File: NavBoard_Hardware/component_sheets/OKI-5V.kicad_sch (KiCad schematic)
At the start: 4 parts, among them U1 OKI-5V

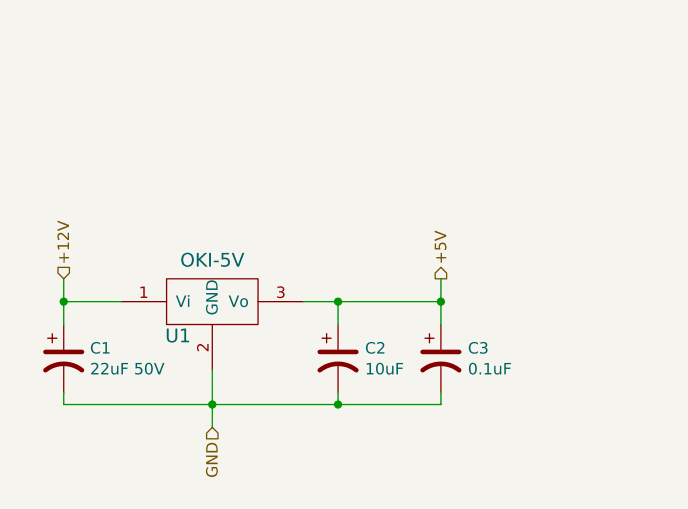
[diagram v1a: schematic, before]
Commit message: Added Information To Voltage Regulator Component Sheets, Improved Schematic Review 1 Powerpoint
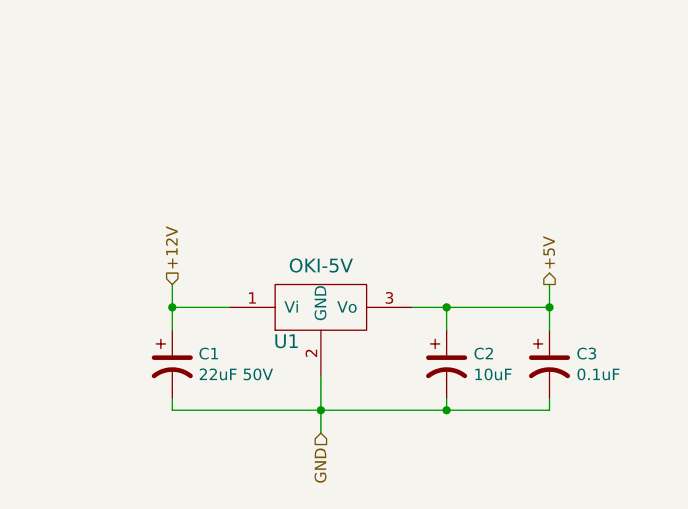
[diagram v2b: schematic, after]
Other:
- company: (none) -> Missouri S&T Mars Rover Design Team
- title: (none) -> OKI 5V Voltage Regulator
- moved on the sheet: C1, C2, C3, U1
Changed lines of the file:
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@@
 (kicad_sch (version 20211123) (generator eeschema)
   (paper "A4")
-  (junction (at 146.05 101.6) (diameter 0) (color 0 0 0 0)
+  (title_block
+    (title "OKI 5V Voltage Regulator")
+    (company "Missouri S&T Mars Rover Design Team")
+    (comment 1 "OKI 5V Voltage Regulator")
+    (comment 2 "Provides Stable 5V From 12V Input")
   )
-  (junction (at 146.05 90.17) (diameter 0) (color 0 0 0 0)
+  (junction (at 158.115 102.235) (diameter 0) (color 0 0 0 0)
   )
-  (junction (at 132.08 101.6) (diameter 0) (color 0 0 0 0)
+  (junction (at 158.115 90.805) (diameter 0) (color 0 0 0 0)
   )
-  (junction (at 115.57 90.17) (diameter 0) (color 0 0 0 0)
+  (junction (at 144.145 102.235) (diameter 0) (color 0 0 0 0)
   )
-  (junction (at 157.48 90.17) (diameter 0) (color 0 0 0 0)
+  (junction (at 127.635 90.805) (diameter 0) (color 0 0 0 0)
   )
-  (wire (pts (xy 115.57 87.63) (xy 115.57 90.17))
+  (junction (at 169.545 90.805) (diameter 0) (color 0 0 0 0)
+  )
+  (wire (pts (xy 127.635 88.265) (xy 127.635 90.805))
     (stroke (width 0) (type default) (color 0 0 0 0))
   )
-  (wire (pts (xy 157.48 101.6) (xy 157.48 100.33))
+  (wire (pts (xy 169.545 102.235) (xy 169.545 100.965))
     (stroke (width 0) (type default) (color 0 0 0 0))
   )
-  (wire (pts (xy 115.57 100.33) (xy 115.57 101.6))
+  (wire (pts (xy 127.635 100.965) (xy 127.635 102.235))
     (stroke (width 0) (type default) (color 0 0 0 0))
   )
-  (wire (pts (xy 146.05 101.6) (xy 157.48 101.6))
+  (wire (pts (xy 158.115 102.235) (xy 169.545 102.235))
     (stroke (width 0) (type default) (color 0 0 0 0))
   )
-  (wire (pts (xy 132.08 101.6) (xy 146.05 101.6))
+  (wire (pts (xy 144.145 102.235) (xy 158.115 102.235))
     (stroke (width 0) (type default) (color 0 0 0 0))
   )
-  (wire (pts (xy 132.08 101.6) (xy 132.08 104.14))
+  (wire (pts (xy 144.145 102.235) (xy 144.145 104.775))
     (stroke (width 0) (type default) (color 0 0 0 0))
   )
-  (wire (pts (xy 121.92 90.17) (xy 115.57 90.17))
+  (wire (pts (xy 133.985 90.805) (xy 127.635 90.805))
     (stroke (width 0) (type default) (color 0 0 0 0))
   )
-  (wire (pts (xy 157.48 92.71) (xy 157.48 90.17))
+  (wire (pts (xy 169.545 93.345) (xy 169.545 90.805))
     (stroke (width 0) (type default) (color 0 0 0 0))
   )
-  (wire (pts (xy 115.57 101.6) (xy 132.08 101.6))
+  (wire (pts (xy 127.635 102.235) (xy 144.145 102.235))
     (stroke (width 0) (type default) (color 0 0 0 0))
   )
-  (wire (pts (xy 157.48 90.17) (xy 157.48 87.63))
+  (wire (pts (xy 169.545 90.805) (xy 169.545 88.265))
     (stroke (width 0) (type default) (color 0 0 0 0))
   )
-  (wire (pts (xy 146.05 92.71) (xy 146.05 90.17))
+  (wire (pts (xy 158.115 93.345) (xy 158.115 90.805))
     (stroke (width 0) (type default) (color 0 0 0 0))
   )
-  (wire (pts (xy 132.08 97.79) (xy 132.08 101.6))
+  (wire (pts (xy 144.145 98.425) (xy 144.145 102.235))
     (stroke (width 0) (type default) (color 0 0 0 0))
   )
-  (wire (pts (xy 146.05 90.17) (xy 157.48 90.17))
+  (wire (pts (xy 158.115 90.805) (xy 169.545 90.805))
     (stroke (width 0) (type default) (color 0 0 0 0))
   )
-  (wire (pts (xy 146.05 101.6) (xy 146.05 100.33))
+  (wire (pts (xy 158.115 102.235) (xy 158.115 100.965))
     (stroke (width 0) (type default) (color 0 0 0 0))
   )
-  (wire (pts (xy 115.57 90.17) (xy 115.57 92.71))
+  (wire (pts (xy 127.635 90.805) (xy 127.635 93.345))
     (stroke (width 0) (type default) (color 0 0 0 0))
   )
-  (wire (pts (xy 142.24 90.17) (xy 146.05 90.17))
+  (wire (pts (xy 154.305 90.805) (xy 158.115 90.805))
     (stroke (width 0) (type default) (color 0 0 0 0))
   )
-  (hierarchical_label "GND" (shape input) (at 132.08 104.14 270)
+  (hierarchical_label "GND" (shape input) (at 144.145 104.775 270)
     (effects (font (size 1.27 1.27)) (justify right))
   )
-  (hierarchical_label "+5V" (shape output) (at 157.48 87.63 90)
+  (hierarchical_label "+5V" (shape output) (at 169.545 88.265 90)
     (effects (font (size 1.27 1.27)) (justify left))
   )
-  (hierarchical_label "+12V" (shape input) (at 115.57 87.63 90)
+  (hierarchical_label "+12V" (shape input) (at 127.635 88.265 90)
     (effects (font (size 1.27 1.27)) (justify left))
   )
-  (symbol (lib_id "Device:C_Polarized_US") (at 115.57 96.52 0) (unit 1)
+  (symbol (lib_id "Device:C_Polarized_US") (at 127.635 97.155 0) (unit 1)
     (in_bom yes) (on_board yes)
-    (property "Reference" "C1" (id 0) (at 118.491 95.3516 0)
+    (property "Reference" "C1" (id 0) (at 130.556 95.9866 0)
       (effects (font (size 1.27 1.27)) (justify left))
     )
-    (property "Value" "22uF 50V" (id 1) (at 118.491 97.663 0)
+    (property "Value" "22uF 50V" (id 1) (at 130.556 98.298 0)
       (effects (font (size 1.27 1.27)) (justify left))
     )
-    (property "Footprint" "Capacitor_THT:CP_Radial_D6.3mm_P2.50mm" (id 2) (at 115.57 96.52 0)
+    (property "Footprint" "Capacitor_THT:CP_Radial_D6.3mm_P2.50mm" (id 2) (at 127.635 97.155 0)
       (effects (font (size 1.27 1.27)) hide)
     )
-    (property "Datasheet" "~" (id 3) (at 115.57 96.52 0)
+    (property "Datasheet" "~" (id 3) (at 127.635 97.155 0)
       (effects (font (size 1.27 1.27)) hide)
     )
@@
     (pin "2")
   )
-  (symbol (lib_id "Device:C_Polarized_US") (at 146.05 96.52 0) (unit 1)
+  (symbol (lib_id "Device:C_Polarized_US") (at 158.115 97.155 0) (unit 1)
     (in_bom yes) (on_board yes)
-    (property "Reference" "C2" (id 0) (at 149.0472 95.3516 0)
+    (property "Reference" "C2" (id 0) (at 161.1122 95.9866 0)
       (effects (font (size 1.27 1.27)) (justify left))
     )
-    (property "Value" "10uF" (id 1) (at 149.0472 97.663 0)
+    (property "Value" "10uF" (id 1) (at 161.1122 98.298 0)
       (effects (font (size 1.27 1.27)) (justify left))
     )
-    (property "Footprint" "Capacitor_SMD:C_0603_1608Metric_Pad1.08x0.95mm_HandSolder" (id 2) (at 146.05 96.52 0)
+    (property "Footprint" "Capacitor_SMD:C_0603_1608Metric_Pad1.08x0.95mm_HandSolder" (id 2) (at 158.115 97.155 0)
       (effects (font (size 1.27 1.27)) hide)
     )
-    (property "Datasheet" "~" (id 3) (at 146.05 96.52 0)
+    (property "Datasheet" "~" (id 3) (at 158.115 97.155 0)
       (effects (font (size 1.27 1.27)) hide)
     )
@@
     (pin "2")
   )
-  (symbol (lib_id "Device:C_Polarized_US") (at 157.48 96.52 0) (unit 1)
+  (symbol (lib_id "Device:C_Polarized_US") (at 169.545 97.155 0) (unit 1)
     (in_bom yes) (on_board yes)
-    (property "Reference" "C3" (id 0) (at 160.4772 95.3516 0)
+    (property "Reference" "C3" (id 0) (at 172.5422 95.9866 0)
       (effects (font (size 1.27 1.27)) (justify left))
     )
-    (property "Value" "0.1uF" (id 1) (at 160.4772 97.663 0)
+    (property "Value" "0.1uF" (id 1) (at 172.5422 98.298 0)
       (effects (font (size 1.27 1.27)) (justify left))
     )
-    (property "Footprint" "Capacitor_SMD:C_0603_1608Metric_Pad1.08x0.95mm_HandSolder" (id 2) (at 157.48 96.52 0)
+    (property "Footprint" "Capacitor_SMD:C_0603_1608Metric_Pad1.08x0.95mm_HandSolder" (id 2) (at 169.545 97.155 0)
       (effects (font (size 1.27 1.27)) hide)
     )
-    (property "Datasheet" "~" (id 3) (at 157.48 96.52 0)
+    (property "Datasheet" "~" (id 3) (at 169.545 97.155 0)
       (effects (font (size 1.27 1.27)) hide)
     )
@@
     (pin "2")
   )
-  (symbol (lib_id "MRDT_Devices:OKI") (at 127 92.71 0) (unit 1)
+  (symbol (lib_id "MRDT_Devices:OKI") (at 139.065 93.345 0) (unit 1)
     (in_bom yes) (on_board yes)
-    (property "Reference" "U1" (id 0) (at 128.27 93.98 0)
+    (property "Reference" "U1" (id 0) (at 140.335 94.615 0)
       (effects (font (size 1.524 1.524)))
     )
-    (property "Value" "OKI-5V" (id 1) (at 132.08 85.5726 0)
+    (property "Value" "OKI-5V" (id 1) (at 144.145 86.2076 0)
       (effects (font (size 1.524 1.524)))
     )
-    (property "Footprint" "MRDT_Devices:OKI_Horizontal" (id 2) (at 121.92 95.25 0)
+    (property "Footprint" "MRDT_Devices:OKI_Horizontal" (id 2) (at 133.985 95.885 0)
       (effects (font (size 1.524 1.524)) hide)
     )
-    (property "Datasheet" "" (id 3) (at 121.92 95.25 0)
+    (property "Datasheet" "" (id 3) (at 133.985 95.885 0)
       (effects (font (size 1.524 1.524)) hide)
     )

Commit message: Updated sheet title info
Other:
- company: Missouri S&T Mars Rover Design Team -> Thomas Francois, Katherine Dunlap, Missouri S&T Mars Rover Design Team
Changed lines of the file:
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@@
   (title_block
     (title "OKI 5V Voltage Regulator")
-    (company "Missouri S&T Mars Rover Design Team")
+    (company "Thomas Francois, Katherine Dunlap, Missouri S&T Mars Rover Design Team")
     (comment 1 "OKI 5V Voltage Regulator")
     (comment 2 "Provides Stable 5V From 12V Input")

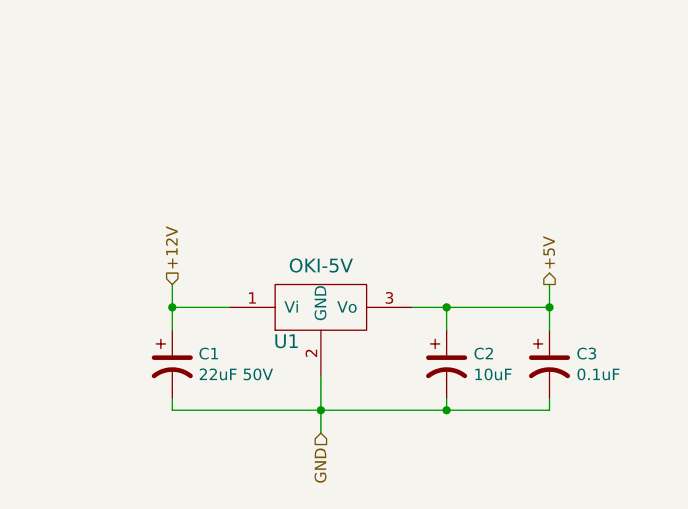
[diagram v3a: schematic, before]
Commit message: Added signage for TSR power supplies
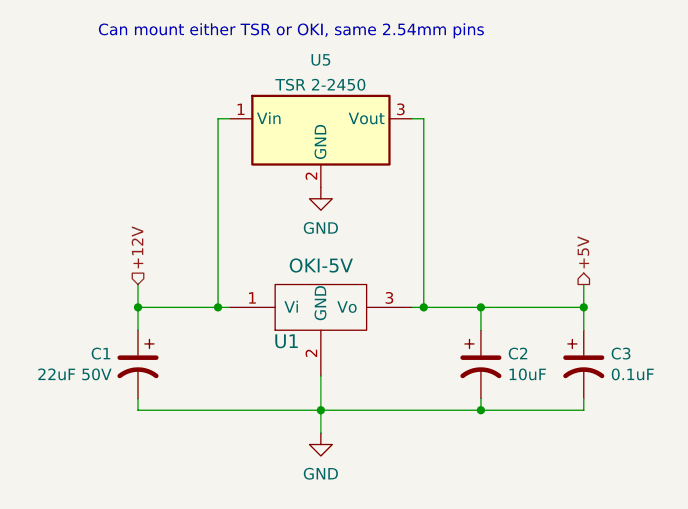
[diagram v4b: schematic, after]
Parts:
- added U5: TSR 2-2450, Converter_DCDC:Converter_DCDC_TRACO_TSR-1_THT, symbol Regulator_Switching:TSR_1-2412
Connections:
- net +12V: now also U5.1 (Vin)
- net +5V: now also U5.3 (Vout)
- net GND: now also U5.2 (GND)
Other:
- note added: "Can mount either TSR or OKI, same 2.54mm pins"
- moved on the sheet: C1, C2, C3
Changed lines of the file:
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@@
     (comment 2 "Provides Stable 5V From 12V Input")
   )
-  (junction (at 158.115 102.235) (diameter 0) (color 0 0 0 0)
+  (junction (at 161.925 102.235) (diameter 0) (color 0 0 0 0)
   )
-  (junction (at 158.115 90.805) (diameter 0) (color 0 0 0 0)
+  (junction (at 161.925 90.805) (diameter 0) (color 0 0 0 0)
+  )
+  (junction (at 132.715 90.805) (diameter 0) (color 0 0 0 0)
   )
   (junction (at 144.145 102.235) (diameter 0) (color 0 0 0 0)
   )
-  (junction (at 127.635 90.805) (diameter 0) (color 0 0 0 0)
+  (junction (at 123.825 90.805) (diameter 0) (color 0 0 0 0)
   )
-  (junction (at 169.545 90.805) (diameter 0) (color 0 0 0 0)
+  (junction (at 173.355 90.805) (diameter 0) (color 0 0 0 0)
   )
-  (wire (pts (xy 127.635 88.265) (xy 127.635 90.805))
+  (junction (at 155.575 90.805) (diameter 0) (color 0 0 0 0)
+  )
+  (wire (pts (xy 154.305 69.85) (xy 155.575 69.85))
     (stroke (width 0) (type default) (color 0 0 0 0))
   )
-  (wire (pts (xy 169.545 102.235) (xy 169.545 100.965))
+  (wire (pts (xy 155.575 90.805) (xy 161.925 90.805))
     (stroke (width 0) (type default) (color 0 0 0 0))
   )
-  (wire (pts (xy 127.635 100.965) (xy 127.635 102.235))
+  (wire (pts (xy 123.825 88.265) (xy 123.825 90.805))
     (stroke (width 0) (type default) (color 0 0 0 0))
   )
-  (wire (pts (xy 158.115 102.235) (xy 169.545 102.235))
+  (wire (pts (xy 173.355 102.235) (xy 173.355 100.965))
     (stroke (width 0) (type default) (color 0 0 0 0))
   )
-  (wire (pts (xy 144.145 102.235) (xy 158.115 102.235))
+  (wire (pts (xy 123.825 100.965) (xy 123.825 102.235))
+    (stroke (width 0) (type default) (color 0 0 0 0))
+  )
+  (wire (pts (xy 161.925 102.235) (xy 173.355 102.235))
+    (stroke (width 0) (type default) (color 0 0 0 0))
+  )
+  (wire (pts (xy 144.145 102.235) (xy 161.925 102.235))
     (stroke (width 0) (type default) (color 0 0 0 0))
   )
@@
     (stroke (width 0) (type default) (color 0 0 0 0))
   )
-  (wire (pts (xy 133.985 90.805) (xy 127.635 90.805))
+  (wire (pts (xy 133.985 69.85) (xy 132.715 69.85))
     (stroke (width 0) (type default) (color 0 0 0 0))
   )
-  (wire (pts (xy 169.545 93.345) (xy 169.545 90.805))
+  (wire (pts (xy 155.575 69.85) (xy 155.575 90.805))
     (stroke (width 0) (type default) (color 0 0 0 0))
   )
-  (wire (pts (xy 127.635 102.235) (xy 144.145 102.235))
+  (wire (pts (xy 173.355 93.345) (xy 173.355 90.805))
     (stroke (width 0) (type default) (color 0 0 0 0))
   )
-  (wire (pts (xy 169.545 90.805) (xy 169.545 88.265))
+  (wire (pts (xy 123.825 102.235) (xy 144.145 102.235))
     (stroke (width 0) (type default) (color 0 0 0 0))
   )
-  (wire (pts (xy 158.115 93.345) (xy 158.115 90.805))
+  (wire (pts (xy 132.715 69.85) (xy 132.715 90.805))
+    (stroke (width 0) (type default) (color 0 0 0 0))
+  )
+  (wire (pts (xy 173.355 90.805) (xy 173.355 88.265))
+    (stroke (width 0) (type default) (color 0 0 0 0))
+  )
+  (wire (pts (xy 123.825 90.805) (xy 132.715 90.805))
+    (stroke (width 0) (type default) (color 0 0 0 0))
+  )
+  (wire (pts (xy 161.925 93.345) (xy 161.925 90.805))
     (stroke (width 0) (type default) (color 0 0 0 0))
   )
@@
     (stroke (width 0) (type default) (color 0 0 0 0))
   )
-  (wire (pts (xy 158.115 90.805) (xy 169.545 90.805))
+  (wire (pts (xy 161.925 90.805) (xy 173.355 90.805))
     (stroke (width 0) (type default) (color 0 0 0 0))
   )
-  (wire (pts (xy 158.115 102.235) (xy 158.115 100.965))
+  (wire (pts (xy 161.925 102.235) (xy 161.925 100.965))
     (stroke (width 0) (type default) (color 0 0 0 0))
   )
-  (wire (pts (xy 127.635 90.805) (xy 127.635 93.345))
+  (wire (pts (xy 123.825 90.805) (xy 123.825 93.345))
     (stroke (width 0) (type default) (color 0 0 0 0))
   )
-  (wire (pts (xy 154.305 90.805) (xy 158.115 90.805))
+  (wire (pts (xy 132.715 90.805) (xy 133.985 90.805))
     (stroke (width 0) (type default) (color 0 0 0 0))
   )
-  (hierarchical_label "GND" (shape input) (at 144.145 104.775 270)
-    (effects (font (size 1.27 1.27)) (justify right))
+  (wire (pts (xy 154.305 90.805) (xy 155.575 90.805))
+    (stroke (width 0) (type default) (color 0 0 0 0))
   )
-  (hierarchical_label "+5V" (shape output) (at 169.545 88.265 90)
+  (text "Can mount either TSR or OKI, same 2.54mm pins" (at 119.38 60.96 0)
+    (effects (font (size 1.27 1.27)) (justify left bottom))
+  )
+  (hierarchical_label "+5V" (shape output) (at 173.355 88.265 90)
     (effects (font (size 1.27 1.27)) (justify left))
   )
-  (hierarchical_label "+12V" (shape input) (at 127.635 88.265 90)
+  (hierarchical_label "+12V" (shape input) (at 123.825 88.265 90)
     (effects (font (size 1.27 1.27)) (justify left))
   )
-  (symbol (lib_id "Device:C_Polarized_US") (at 127.635 97.155 0) (unit 1)
+  (symbol (lib_id "Device:C_Polarized_US") (at 123.825 97.155 0) (mirror y) (unit 1)
     (in_bom yes) (on_board yes)
-    (property "Reference" "C1" (id 0) (at 130.556 95.9866 0)
+    (property "Reference" "C1" (id 0) (at 120.904 95.9866 0)
       (effects (font (size 1.27 1.27)) (justify left))
     )
-    (property "Value" "22uF 50V" (id 1) (at 130.556 98.298 0)
+    (property "Value" "22uF 50V" (id 1) (at 120.904 98.298 0)
       (effects (font (size 1.27 1.27)) (justify left))
     )
-    (property "Footprint" "Capacitor_THT:CP_Radial_D6.3mm_P2.50mm" (id 2) (at 127.635 97.155 0)
+    (property "Footprint" "Capacitor_THT:CP_Radial_D6.3mm_P2.50mm" (id 2) (at 123.825 97.155 0)
       (effects (font (size 1.27 1.27)) hide)
     )
-    (property "Datasheet" "~" (id 3) (at 127.635 97.155 0)
+    (property "Datasheet" "~" (id 3) (at 123.825 97.155 0)
       (effects (font (size 1.27 1.27)) hide)
     )
@@
     (pin "2")
   )
-  (symbol (lib_id "Device:C_Polarized_US") (at 158.115 97.155 0) (unit 1)
+  (symbol (lib_id "Device:C_Polarized_US") (at 161.925 97.155 0) (unit 1)
     (in_bom yes) (on_board yes)
-    (property "Reference" "C2" (id 0) (at 161.1122 95.9866 0)
+    (property "Reference" "C2" (id 0) (at 164.9222 95.9866 0)
       (effects (font (size 1.27 1.27)) (justify left))
     )
-    (property "Value" "10uF" (id 1) (at 161.1122 98.298 0)
+    (property "Value" "10uF" (id 1) (at 164.9222 98.298 0)
       (effects (font (size 1.27 1.27)) (justify left))
     )
-    (property "Footprint" "Capacitor_SMD:C_0603_1608Metric_Pad1.08x0.95mm_HandSolder" (id 2) (at 158.115 97.155 0)
+    (property "Footprint" "Capacitor_SMD:C_0603_1608Metric_Pad1.08x0.95mm_HandSolder" (id 2) (at 161.925 97.155 0)
       (effects (font (size 1.27 1.27)) hide)
     )
-    (property "Datasheet" "~" (id 3) (at 158.115 97.155 0)
+    (property "Datasheet" "~" (id 3) (at 161.925 97.155 0)
       (effects (font (size 1.27 1.27)) hide)
     )
@@
     (pin "2")
   )
-  (symbol (lib_id "Device:C_Polarized_US") (at 169.545 97.155 0) (unit 1)
+  (symbol (lib_id "power:GND") (at 144.145 77.47 0) (unit 1)
+    (in_bom yes) (on_board yes) (fields_autoplaced)
+    (property "Reference" "#PWR014" (id 0) (at 144.145 83.82 0)
+      (effects (font (size 1.27 1.27)) hide)
+    )
+    (property "Value" "GND" (id 1) (at 144.145 82.0325 0))
+    (property "Footprint" "" (id 2) (at 144.145 77.47 0)
+      (effects (font (size 1.27 1.27)) hide)
+    )
+    (property "Datasheet" "" (id 3) (at 144.145 77.47 0)
+      (effects (font (size 1.27 1.27)) hide)
+    )
+    (pin "1")
+  )
+  (symbol (lib_id "Device:C_Polarized_US") (at 173.355 97.155 0) (unit 1)
     (in_bom yes) (on_board yes)
-    (property "Reference" "C3" (id 0) (at 172.5422 95.9866 0)
+    (property "Reference" "C3" (id 0) (at 176.3522 95.9866 0)
       (effects (font (size 1.27 1.27)) (justify left))
     )
-    (property "Value" "0.1uF" (id 1) (at 172.5422 98.298 0)
+    (property "Value" "0.1uF" (id 1) (at 176.3522 98.298 0)
       (effects (font (size 1.27 1.27)) (justify left))
     )
-    (property "Footprint" "Capacitor_SMD:C_0603_1608Metric_Pad1.08x0.95mm_HandSolder" (id 2) (at 169.545 97.155 0)
+    (property "Footprint" "Capacitor_SMD:C_0603_1608Metric_Pad1.08x0.95mm_HandSolder" (id 2) (at 173.355 97.155 0)
       (effects (font (size 1.27 1.27)) hide)
     )
-    (property "Datasheet" "~" (id 3) (at 169.545 97.155 0)
+    (property "Datasheet" "~" (id 3) (at 173.355 97.155 0)
       (effects (font (size 1.27 1.27)) hide)
     )
     (pin "1")
     (pin "2")
+  )
+  (symbol (lib_id "power:GND") (at 144.145 104.775 0) (unit 1)
+    (in_bom yes) (on_board yes) (fields_autoplaced)
+    (property "Reference" "#PWR015" (id 0) (at 144.145 111.125 0)
+      (effects (font (size 1.27 1.27)) hide)
+    )
+    (property "Value" "GND" (id 1) (at 144.145 109.3375 0))
+    (property "Footprint" "" (id 2) (at 144.145 104.775 0)
+      (effects (font (size 1.27 1.27)) hide)
+    )
+    (property "Datasheet" "" (id 3) (at 144.145 104.775 0)
+      (effects (font (size 1.27 1.27)) hide)
+    )
+    (pin "1")
   )
   (symbol (lib_id "MRDT_Devices:OKI") (at 139.065 93.345 0) (unit 1)
@@
     )
     (pin "1")
+    (pin "2")
+    (pin "3")
+  )
+  (symbol (lib_id "Regulator_Switching:TSR_1-2412") (at 144.145 72.39 0) (unit 1)
+    (in_bom yes) (on_board yes) (fields_autoplaced)
+    (property "Reference" "U5" (id 0) (at 144.145 63.3435 0))
+    (property "Value" "TSR 2-2450" (id 1) (at 144.145 66.1186 0))
+    (property "Footprint" "Converter_DCDC:Converter_DCDC_TRACO_TSR-1_THT" (id 2) (at 144.145 76.2 0)
+      (effects (font (size 1.27 1.27) italic) (justify left) hide)
+    )
+    (property "Datasheet" "http://www.tracopower.com/products/tsr1.pdf" (id 3) (at 144.145 72.39 0)
+      (effects (font (size 1.27 1.27)) hide)
+    )
+    (pin "1")
